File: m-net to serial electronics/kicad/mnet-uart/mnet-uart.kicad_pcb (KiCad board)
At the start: 2 copper layers, 55.9 x 43.2 mm, 21 parts, among them J1 Screw_Terminal_01x02, J2 Screw_Terminal_01x02, Q1 2N7002K, U1 LM741, U2 LM741, U3 74LS04, U4 NA555P

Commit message: minor
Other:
- board text added: "Input M-NET"
- board text added: "Output 3.3 TTL"
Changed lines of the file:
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@@
     (property "Sheetname" "")
     (attr through_hole)
-    (fp_text reference "J1" (at -3.805 0) (layer "F.SilkS")
+    (fp_text reference "J1" (at -3.805 0) (layer "B.Fab")
       (effects (font (size 1 1) (thickness 0.15)))
     )
@@
     (property "Sheetname" "")
     (attr through_hole)
-    (fp_text reference "J2" (at -4.445 0) (layer "F.SilkS")
+    (fp_text reference "J2" (at -4.445 0) (layer "B.Fab")
       (effects (font (size 1 1) (thickness 0.15)))
     )
@@
   (gr_arc (start 110.49 97.79) (mid 113.184077 98.905923) (end 114.3 101.6) (layer "Edge.Cuts") (width 0.1))
   (gr_arc (start 114.3 137.16) (mid 113.184077 139.854077) (end 110.49 140.97) (layer "Edge.Cuts") (width 0.1))
+  (gr_text "Input M-NET" (at 67.31 102.87) (layer "F.SilkS")
+    (effects (font (size 1.5 1.5) (thickness 0.3)))
+  )
+  (gr_text "Output 3.3 TTL" (at 68.072 120.396) (layer "F.SilkS")
+    (effects (font (size 1.5 1.5) (thickness 0.3)))
+  )
   (segment (start 72.395 113.025) (end 72.644 112.776) (width 0.3) (layer "B.Cu") (net 1))
   (segment (start 65.1 113.025) (end 72.395 113.025) (width 0.3) (layer "B.Cu") (net 1))

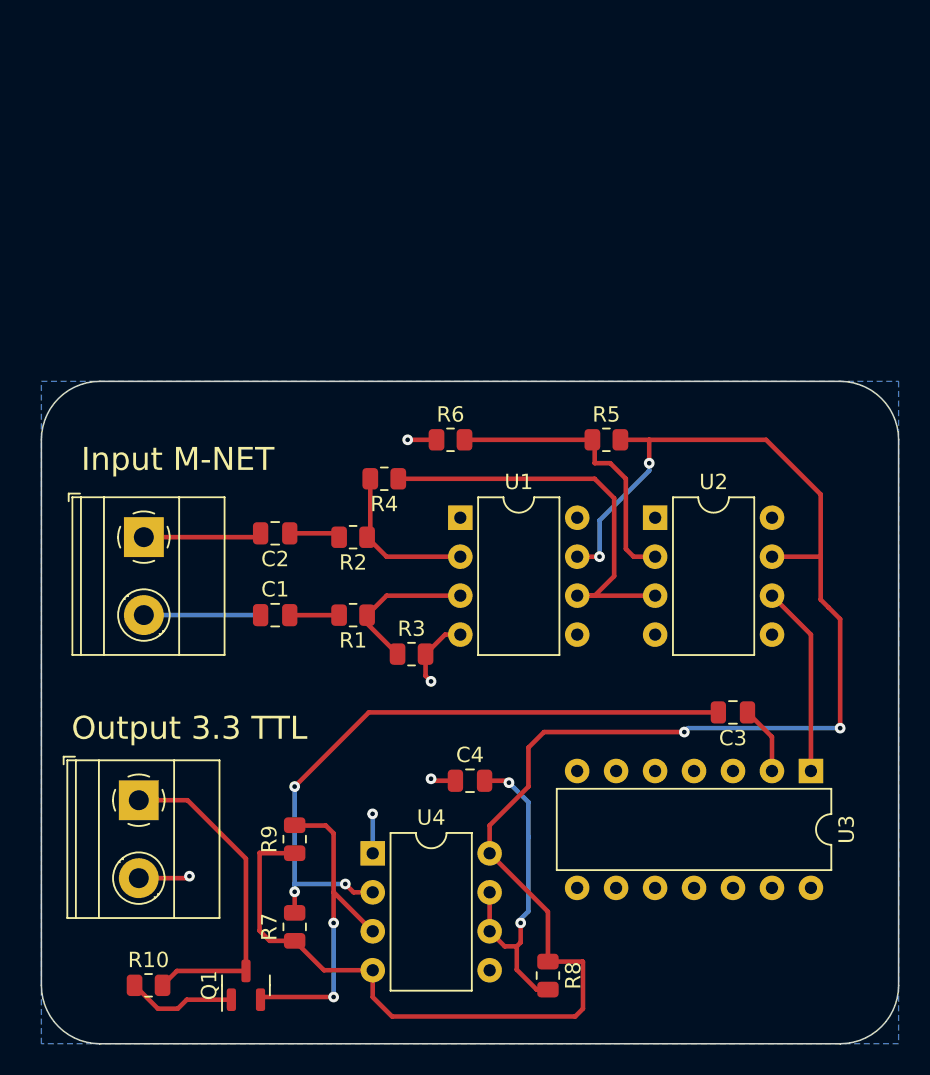
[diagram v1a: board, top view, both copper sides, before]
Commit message: added power supply
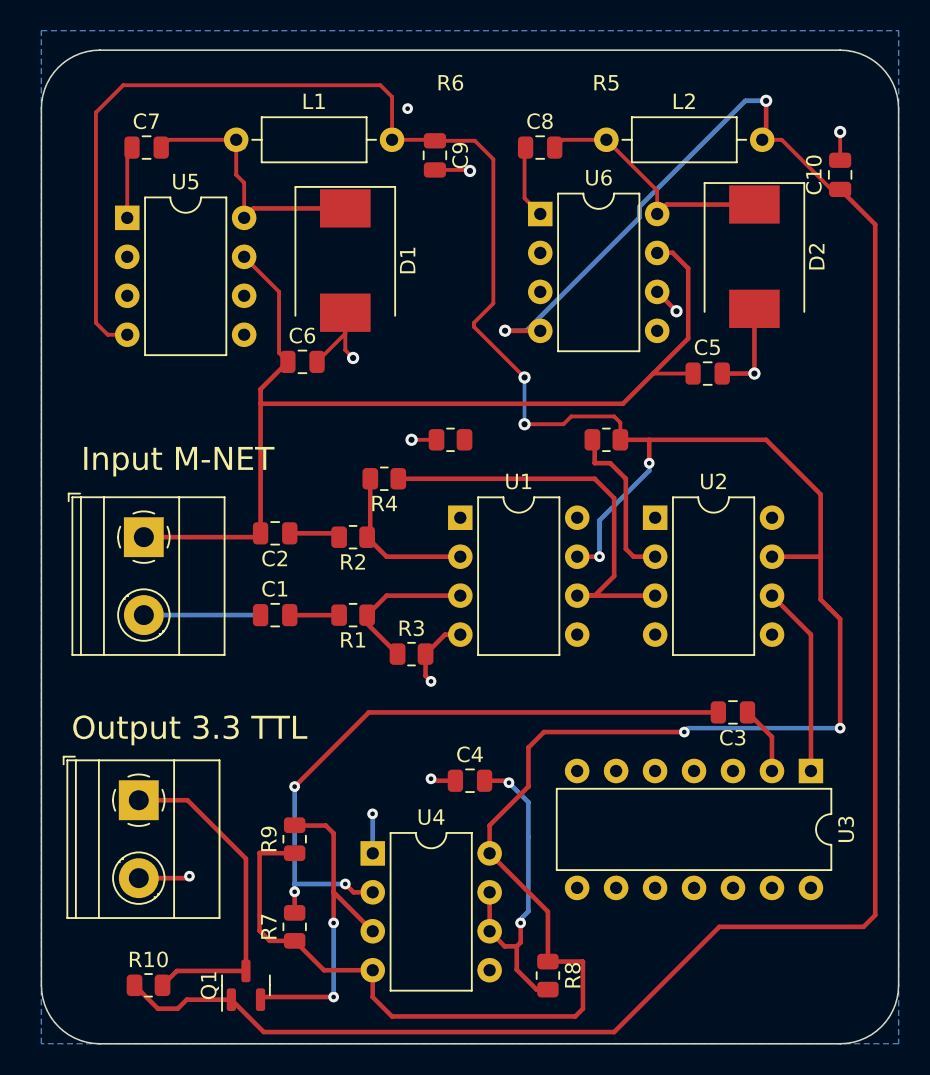
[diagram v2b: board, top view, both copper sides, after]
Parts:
- added C10: 68uF, Capacitor_SMD:C_0805_2012Metric, F.Cu at (110.5, 84.3)
- added C5: 100uF, Capacitor_SMD:C_0805_2012Metric, F.Cu at (101.9, 97.3)
- added C6: 100uF, Capacitor_SMD:C_0805_2012Metric, F.Cu at (75.4, 96.5)
- added C7: 10nF, Capacitor_SMD:C_0805_2012Metric, F.Cu at (65.3, 82.5)
- added C8: 10nF, Capacitor_SMD:C_0805_2012Metric, F.Cu at (90.9, 82.5)
- added C9: 68uF, Capacitor_SMD:C_0805_2012Metric, F.Cu at (84.1, 83.1)
- added D1: B350, Diode_SMD:D_SMC, F.Cu at (78.2, 89.9)
- added D2: B350, Diode_SMD:D_SMC, F.Cu at (104.9, 89.7)
- added L1: INDUCTOR, Inductor_THT:L_Axial_L6.6mm_D2.7mm_P10.16mm_Horizontal_Vishay_IM-2, F.Cu at (71.1, 82.0)
- added L2: INDUCTOR, Inductor_THT:L_Axial_L6.6mm_D2.7mm_P10.16mm_Horizontal_Vishay_IM-2, F.Cu at (95.2, 82.0)
- added U5: LM2672N-5.0, Package_DIP:DIP-8_W7.62mm, F.Cu at (64.0, 87.1)
- added U6: LM2672N-3.3, Package_DIP:DIP-8_W7.62mm, F.Cu at (90.9, 86.9)
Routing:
- net +3.3V: track 7.19 -> 136.5 mm, vias 0 -> 2
- net +5V: track 118.7 -> 191.9 mm, vias 4 -> 6
- net Net-(C2-Pad2): track 7.71 -> 66.9 mm
- net GND: track 14.2 -> 33.3 mm, vias 5 -> 11
- net Net-(C7-Pad2): track 0.00 -> 18.0 mm
- net Net-(C8-Pad2): track 0.00 -> 16.4 mm
- net Net-(R5-Pad1): track 19.1 -> 10.5 mm
- net Net-(C8-Pad1): track 0.00 -> 4.78 mm
- net Net-(C7-Pad1): track 0.00 -> 4.71 mm
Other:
- board size 55.9 x 43.2 mm -> 55.9 x 64.8 mm
